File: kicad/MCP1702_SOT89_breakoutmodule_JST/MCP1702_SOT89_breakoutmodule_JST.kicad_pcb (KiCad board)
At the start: 2 copper layers, 13.6 x 23.5 mm, 9 parts, among them J1 Conn_01x04, J2 Conn_01x02, J3 Conn_01x02, J4 Conn_01x04, U1 MCP1702-MB

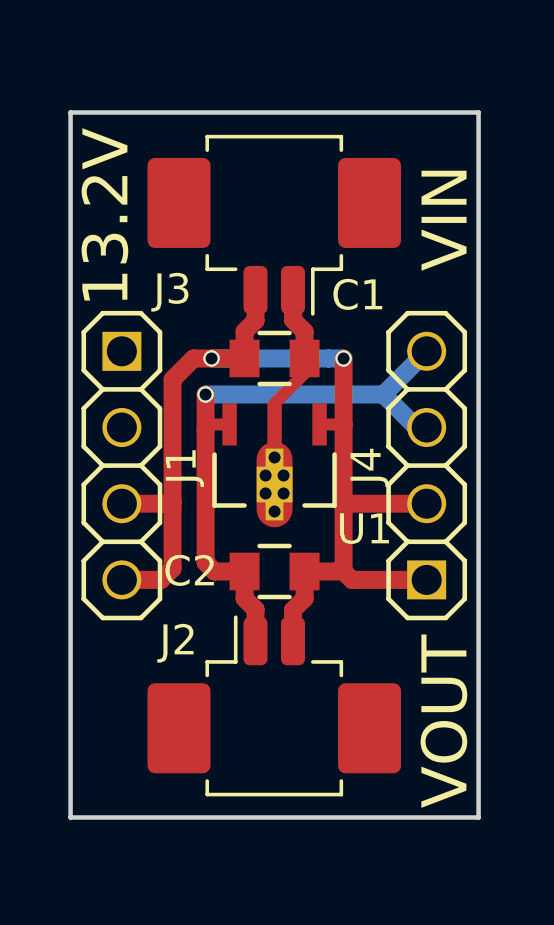
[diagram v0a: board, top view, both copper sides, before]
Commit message: added JST connectors
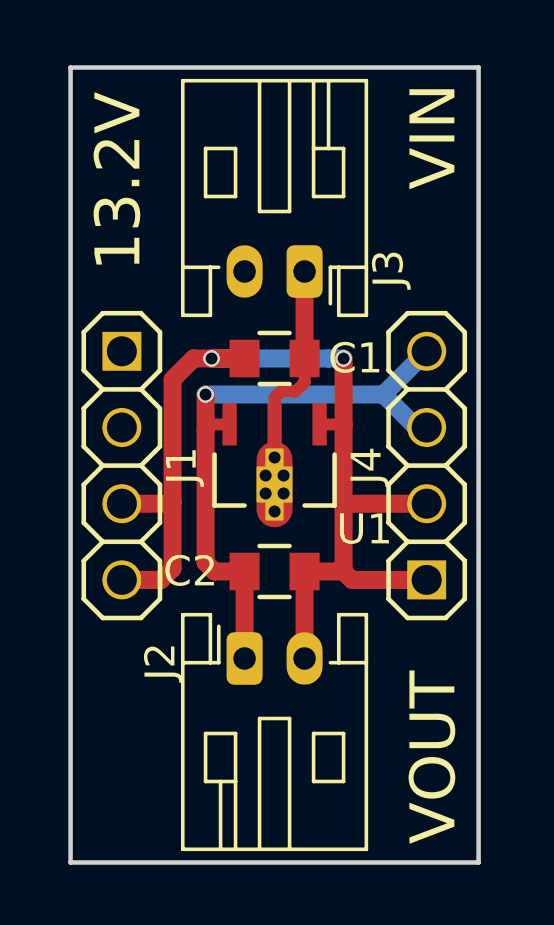
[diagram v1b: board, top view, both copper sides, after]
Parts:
- J2, J3: footprint Connector_Molex:Molex_PicoBlade_53261-0271_1x02-1MP_P1.25mm_Horizontal -> Connector_JST:JST_PH_S2B-PH-K_1x02_P2.00mm_Horizontal
- moved J2 2.08 mm to (134.9, 83.9)
- moved J3 2.05 mm to (136.9, 71.0)
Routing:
- net GND: track 36.7 -> 34.7 mm
- net +12V: track 7.06 -> 7.81 mm
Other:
- board size 13.6 x 23.5 mm -> 13.6 x 26.5 mm

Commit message: updated version number
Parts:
- N2: value 20181110 -> 20181117
- moved N1 8.16 mm to (135.9, 75.0), turned to 180 degrees
- moved N2 4.18 mm to (135.3, 85.9)
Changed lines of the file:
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@@
   )
   (setup
-    (last_trace_width 0.6)
+    (last_trace_width 0.1524)
     (user_trace_width 0.1524)
     (user_trace_width 0.2)
@@
   )
   (module Symbols:OSHW-Symbol_6.7x6mm_SilkScreen (layer B.Cu)
-    (at 134.9 83.1 270)
+    (at 135.9 75 180)
     (descr "Open Source Hardware Symbol")
     (tags "Logo Symbol OSHW")
     (attr virtual)
-    (fp_text reference N1 (at 0 0 270) (layer B.SilkS) hide
+    (fp_text reference N1 (at 0 0 180) (layer B.SilkS) hide
       (effects (font (size 1 1) (thickness 0.15)) (justify mirror))
     )
-    (fp_text value OHWLOGO (at 0.75 0 270) (layer B.Fab) hide
+    (fp_text value OHWLOGO (at 0.75 0 180) (layer B.Fab) hide
       (effects (font (size 1 1) (thickness 0.15)) (justify mirror))
     )
@@
   )
   (module SquantorLabels:Label_version (layer B.Cu)
-    (at 138.4 83.1 90)
+    (at 135.3 85.9 90)
     (fp_text reference N2 (at 0 -1.4 90) (layer B.Fab) hide
       (effects (font (size 1 1) (thickness 0.15)) (justify mirror))
     )
-    (fp_text value 20181110 (at -0.022254 0.35183 270) (layer B.SilkS)
+    (fp_text value 20181117 (at 0 -0.1 180) (layer B.SilkS)
       (effects (font (size 1 1) (thickness 0.15)) (justify mirror))
     )
-    (fp_text user V: (at 4.5 0.35183 270) (layer B.SilkS)
+    (fp_text user V: (at 0 4.4 180) (layer B.SilkS)
       (effects (font (size 1 1) (thickness 0.15)) (justify mirror))
     )
